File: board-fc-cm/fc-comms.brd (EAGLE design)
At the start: 95.9 x 90.2 mm, 258 parts, among them IC1 TXB0108PW, IC10 LNA_COMMON, IC12 TXB0108PW, IC2 LHA1+, IC3 MMZ09332BT1, IC4 PCT2075TP, IC5 PCT2075TP, IC6 MSP430FR2311PW, IC7 CC1125RHBT, IC8 CC1125RHBT, IC9 TXB0108PW, J1 SWD_SHROUD, Q1 8MHz, Q2 BSS84, Q3 32.768kHz, Q4 BSS123, Q5 BSS84, U1 TM4C123[7,G]XXPM, U2 TMP100-EP_DBV_6, U3 TPS3813K33-EP_DBV_6, U4 MPU-9250, U6 TPS79930QDDCRQ1, U7 TPS79930QDDCRQ1, U8 74LVC1G08, X1 BU-SMA-V, X10 BU-SMA-V, X11 BU-SMA-V, X12 BU-SMA-V, X14 BU-SMA-V, X15 BU-SMA-V, X16 BU-SMA-V, X17 BU-SMA-V, X18 SHIELD-26X26, X19 SHIELD-26X26, X2 BU-SMA-V, X20 LFTCXO070, X21 LFTCXO070, X3 BU-SMA-V, X4 BU-SMA-V, X5 BU-SMA-V, X6 BU-SMA-V, X7 BU-SMA-V, X8 BU-SMA-V, X9 BU-SMA-V

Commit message: more routing
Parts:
- moved R1 110.6 mm to (19.2, 80.4), turned to 270 degrees
- moved C95 10.5 mm to (60.8, 10.8)
- moved C50 5.26 mm to (62.0, 46.8), turned to 90 degrees
- moved C54 3.85 mm to (67.1, 29.9), turned to 0 degrees
- moved R22 3.79 mm to (52.0, 69.2), turned to 0 degrees
- moved R23 3.44 mm to (52.0, 70.8), turned to 0 degrees
- moved TP4 3.44 mm to (53.2, 63.2)
- moved C91 3.22 mm to (32.0, 70.8)
- moved C92 3.20 mm to (32.0, 72.8)
- moved C55 3.10 mm to (78.2, 47.2), turned to 180 degrees
- moved TP5 2.56 mm to (55.2, 63.2)
- moved C52 2.53 mm to (72.8, 47.2)
- moved C56 1.79 mm to (75.2, 47.2), turned to 0 degrees
- moved C7 1.44 mm to (62.0, 38.0), turned to 90 degrees
- moved C58 1.41 mm to (65.8, 49.0)
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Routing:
- net WDT_PA_EN: track 0.00 -> 142.8 mm, vias 0 -> 1
- net N$1: track 0.00 -> 142.1 mm, vias 0 -> 1
- net GND: track 139.8 -> 232.1 mm, vias 114 -> 160
- net TMP/SCL: track 0.00 -> 82.1 mm, vias 0 -> 6
- net TMP/SDA: track 0.00 -> 78.9 mm, vias 0 -> 5
- net RX_RST: track 11.5 -> 72.7 mm
- net RX_CLK: track 4.63 -> 64.7 mm
- net RX_MOSI: track 4.80 -> 63.9 mm, vias 2 -> 3
- net RX_MISO: track 6.86 -> 61.0 mm
- net TX_CS: track 12.6 -> 66.1 mm, vias 2 -> 3
- net RX_GPIO0: track 7.28 -> 58.2 mm, vias 2 -> 3
- net RX_CS: track 8.46 -> 59.3 mm
- net TX_RST: track 8.49 -> 56.1 mm, vias 2 -> 3
- net TC/TXRX/MISO: track 0.00 -> 44.3 mm, vias 0 -> 2
- net ANT/GATE: track 0.00 -> 42.4 mm, vias 0 -> 2
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- added copper zone on layer 1, net N$10
- added copper zone on layer 1, net N$3

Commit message: some more routing
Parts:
- removed C87, C88, C89, C90: dnp, passives-7351:C0603-N
- removed L18, L19, L20: 0R, passives-7351:L0603-N
- removed X16, X17: BU-SMA-V, con-coax:BU-SMA-V
- added R31, R32: 4k7, passives-7351:R0603-N
- moved C108 138.9 mm to (56.8, 59.6), turned to 180 degrees
- moved C10 130.8 mm to (56.0, 50.0), turned to 180 degrees
- moved TP16 104.3 mm to (34.3, 6.35), flipped to the bottom, turned to 270 degrees
- moved TP12 99.1 mm to (36.8, 6.35), flipped to the bottom, turned to 270 degrees
- moved TP14 98.1 mm to (31.8, 6.35), flipped to the bottom, turned to 270 degrees
- moved TP15 95.7 mm to (26.7, 6.35), flipped to the bottom, turned to 270 degrees
- moved TP13 93.9 mm to (29.2, 6.35), flipped to the bottom, turned to 270 degrees
- moved TP11 85.8 mm to (24.1, 6.35), flipped to the bottom, turned to 270 degrees
- moved R14 79.2 mm to (10.0, 80.8)
- moved R13 77.1 mm to (10.0, 79.2)
- moved R12 75.3 mm to (10.0, 77.6)
- moved R11 73.7 mm to (10.0, 76.0)
- moved SV5 72.5 mm to (55.6, 2.14), turned to 180 degrees
- moved LED2 64.8 mm to (18.2, 77.0), turned to 90 degrees
- moved LED4 59.9 mm to (6.80, 81.2), turned to 90 degrees
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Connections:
- removed net N$103: JP1.2, Q5.3
- removed net N$42: LED2.A, R12.1
- removed net N$58: R13.2
- removed net N$64: R12.2
- removed net N$65: R11.2
- removed net N$79: C87.2, L18.1, X16.1
- removed net N$80: C88.2, L18.2, L19.1
- removed net N$81: C89.2, L19.2, L20.1
- removed net N$82: C90.2, L20.2, X17.1
- removed net N$88: C98.1, C99.1, IC4.8, IC5.7, IC5.8, R22.2, R23.2
- new net N$2: C64.2, JP1.1, L11.2, LED7.A
- new net N$38: LED1.C, R11.2
- new net N$51: R13.2, U1.46
- net 3V3/FMCU: now also C98.1, C99.1, IC4.8, IC5.7, IC5.8, R22.2, R23.2
- net 3V3/SYS: now also R31.2, R32.2
- net 9AXIS/SCL: now also R32.1
- net 9AXIS/SDA: now also R31.1
- net GND: now also IC12.1, IC12.3, IC12.6, IC12.7, IC12.8, IC12.9, R11.1, R12.1; no longer C87.1, C88.1, C89.1, C90.1, LED1.C, LED2.C, X16.2, X16.3, X16.4, X16.5, X17.2, X17.3, X17.4, X17.5
- net N$41: now also LED2.C, R12.2; no longer LED1.A, R11.1
- net N$49: now also U1.50
- net N$52: now also JP1.2, Q5.3; no longer C64.2, JP1.1, L11.2, LED7.A
- net N$90: now also JP8.3; no longer JP8.4
- net N$91: now also JP8.4; no longer JP8.3
- net TX_GPIO3: now also LED2.A
- net WDT_PA_EN: now also LED1.A
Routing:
- net GND: track 232.1 -> 373.2 mm, vias 160 -> 232
- net 5V/SYS: track 9.59 -> 125.0 mm, vias 0 -> 8
- net 5V/CAM: track 0.00 -> 107.0 mm
- net 3V3/FMCU: track 30.9 -> 127.5 mm, vias 5 -> 12
- net PA_POWER: track 0.00 -> 95.3 mm, vias 0 -> 7
- net N$53: track 104.0 -> 199.2 mm, vias 13 -> 19
- net N$49: track 0.00 -> 93.9 mm, vias 0 -> 2
- net N$51: track 0.00 -> 90.2 mm, vias 0 -> 2
- net N$40: track 112.6 -> 201.7 mm, vias 17 -> 24
- net N$61: track 0.00 -> 80.5 mm, vias 0 -> 2
- net TX_GPIO3: track 2.00 -> 82.4 mm, vias 1 -> 2
- net N$73: track 0.00 -> 79.5 mm, vias 0 -> 2
- net RX_GPIO3: track 2.09 -> 81.3 mm, vias 1 -> 2
- net TX_REG_EN: track 7.76 -> 82.1 mm, vias 1 -> 4
- net SWDIO: track 34.5 -> 88.6 mm, vias 1 -> 3
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- added copper zone on layer 15, net 3V3/FMCU
- added copper zone on layer 15, net 5V/SYS
- added copper zone on layer 2, net 5V/SYS
- added copper zone on layer 2, net GND
- added copper zone on layer 15, net N$24
- added copper zone on layer 15, net N$40
- added copper zone on layer 15, net PA_PWR
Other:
- board text added: "5V"
- board text added: "CAM"
- board text added: "GPIO3"
- board text added: "LNA FET BYPASS"
- board text added: "LNA PWR"
- board text added: "PA"
- board text added: "PA FET BYPASS"
- board text added: "PA PWR"
- board text added: "SYS"
- board text added: "WDT PA EN"

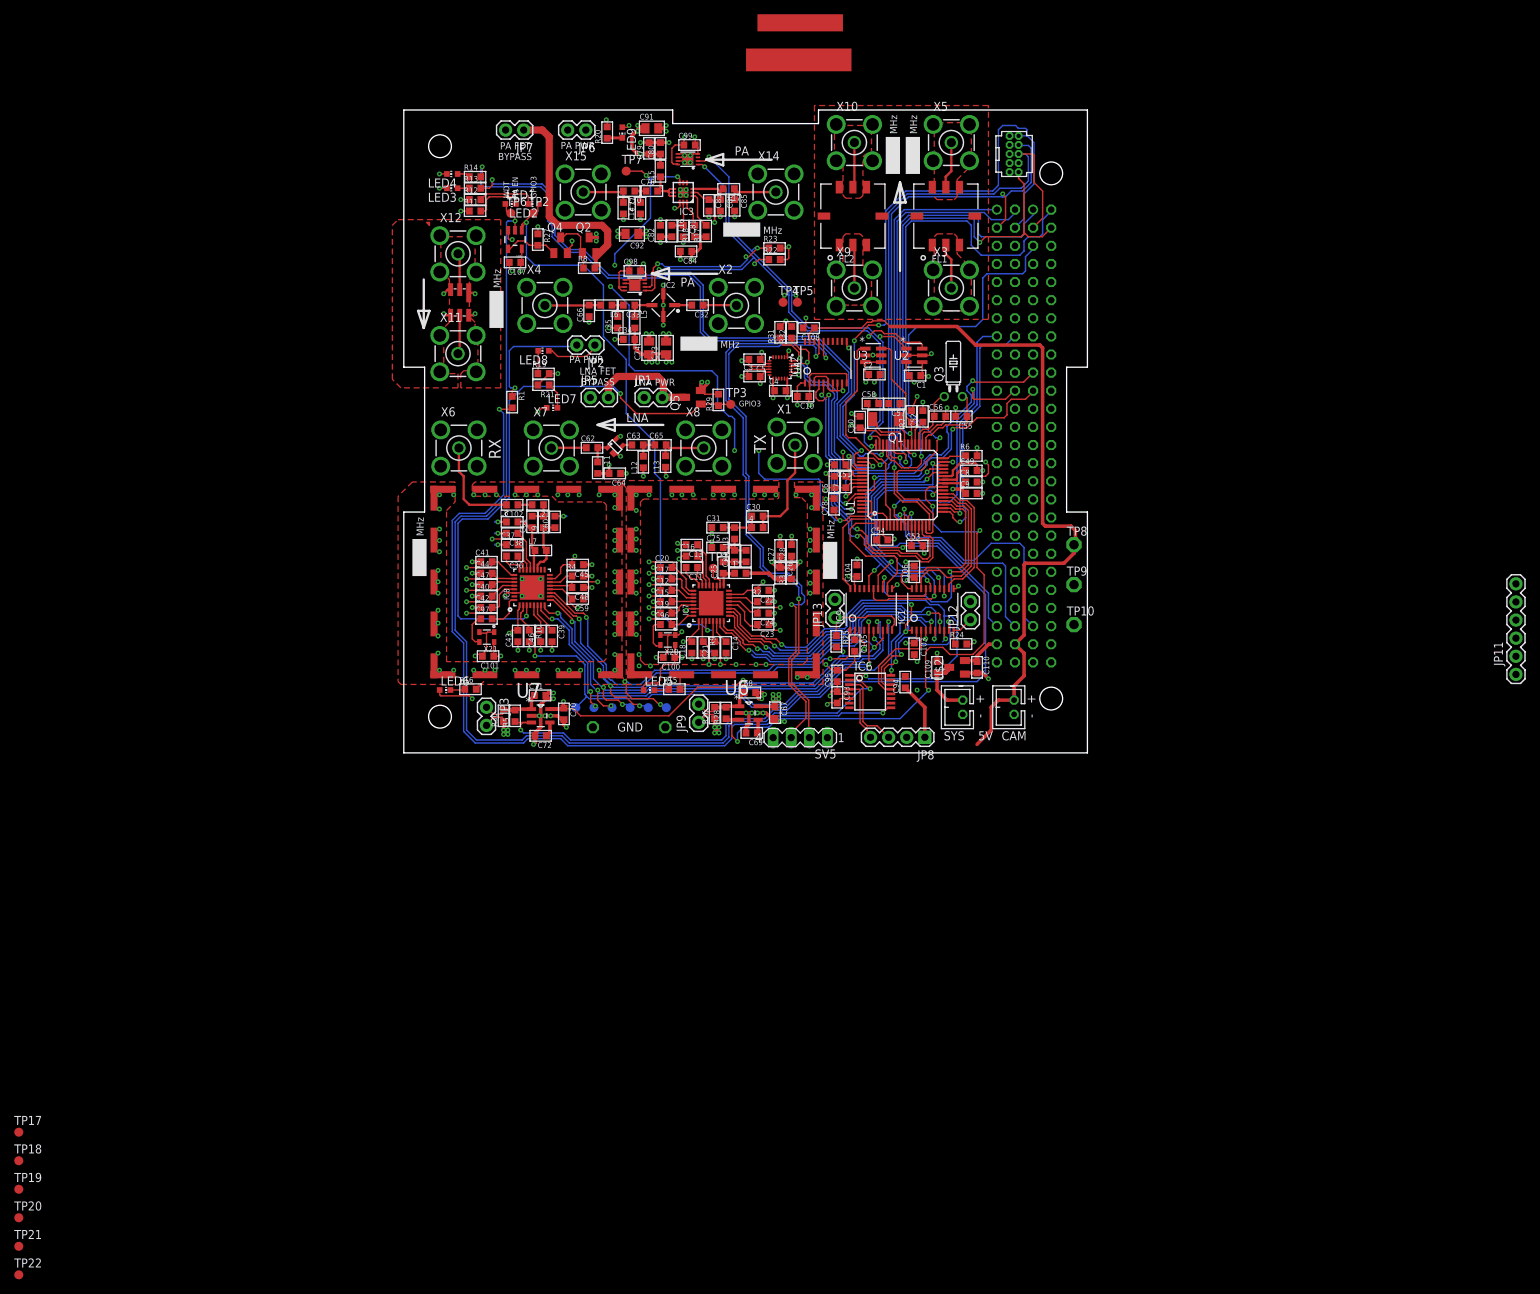
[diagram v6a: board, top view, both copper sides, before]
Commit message: cleaning up silk
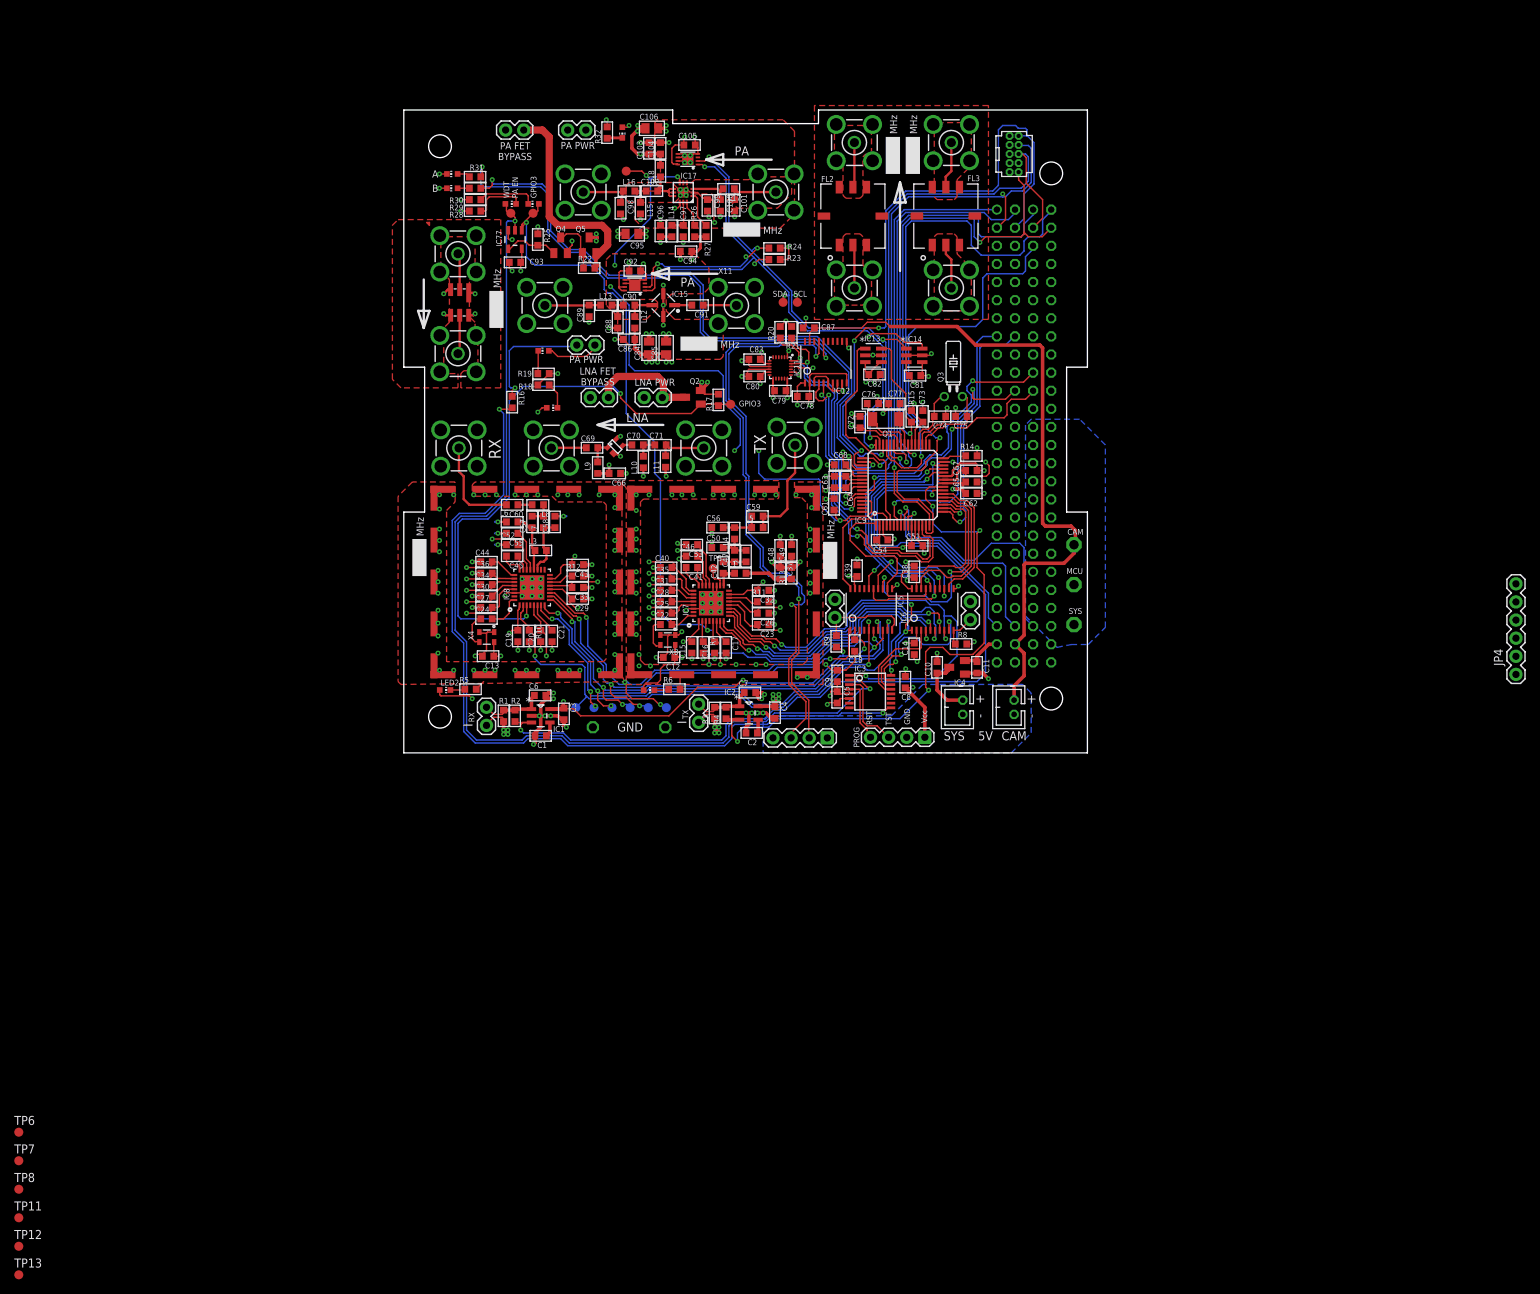
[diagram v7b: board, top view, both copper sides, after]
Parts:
- removed C107: 100n, passives-7351:C0603-N
- removed C109, C110: 4.7u, passives-7351:C0603-N
- removed JP13: M02PTH, SparkFun-Connectors:1X02
- removed L21: 15n, passives-7351:L0603-N
- removed SV5: CAM, con-lstb:MA04-1
- removed U$2: MCP1700TT, dtb:SOT23
- removed U1: TM4C123[7,G]XXPM, ti-tiva:PM_S-PQFP-G64
- removed U6, U7: TPS79930QDDCRQ1, cube-parts:SOT95P280X110-5N
- removed X19: SHIELD-26X26, CubeSat3:SHIELD-26X26
- removed X20, X21: LFTCXO070, CubeSat3:260-SERIES
- added C88, C89: dnp, passives-7351:C0603-N
- added C90: ??, passives-7351:C0603-N
- added IC15: LHA1+, CubeSat3:PA
- added IC16, IC18: PCT2075TP, CubeSat3:HWSON8
- added IC17: MMZ09332BT1, CubeSat3:QFN3X3-6
- added JP10: M02PTH, SparkFun-Connectors:1X02
- added JP4: FTDI_BASICPTH, SparkFun-Connectors:FTDI_BASIC
- added L18: 33n, passives-7351:L0603-N
- added X13, X16, X17: BU-SMA-V, con-coax:BU-SMA-V
- C1, C2: value 0.1u -> 10n
- C10: value 0.1u -> 4.7u
- C100: value 100n -> 27p
- C101: value 100n -> 15p
- C102: value (none) -> 220p
- C103: value 100n -> 4.7u
- C104: value 100n -> 1n
- C106, C95: value 100n -> (none); device passives-7351:C0603-N -> passives-7351:C0805-N
- C11: value 1.8n -> 4.7u
- C12, C18: value 47n -> 100n
- C13, C38: value 10n -> 100n
- C14, C39: value 220n -> 100n
- C17, C21: value 47n -> 220n
- C22, C24: value 47n -> 10n
- C25: value 82p -> 47n
- C26, C27: value 100p -> 47n
- C28: value 10n -> 47n
- C29: value 12p -> 47n
- C3, C4, C6, C7: value 0.1u -> 2u2
- C30: value 1.2p -> 47n
- C31: value 15p -> 47n
- C32: value 1n -> 47n
- C33, C34: value ?? -> 47n
- C35: value dnp -> 47n
- C36: value 1.8n -> 47n
- C37, C48: value 47n -> 100p
- C41, C45: value 47n -> 1.8n
- C42: value 47n -> 82p
- C47: value 47n -> 12p
- C49, C53: value 0.01u -> 10n
- C5: value 0.01u -> 1u
- C50: value 0.1u -> 12p
- C52: value 0.1u -> 47n
- C55: value 24p -> 10n
- C56: value 24p -> 15p
- C57, C58: value 10p -> 5.1p
- C59: value 47n -> 1.2p
- C60: value 5.1p -> (none)
- C61: value 5.1p -> 100p
- C62: value ?? -> 2.2u
- C63, C64: value ?? -> 0.1u
- C65: value 0R -> 1.0u
- C66: value dnp -> ??
- C67, C68: value 2u2 -> 0.01u
- C69: value 10n -> ??
- C70: value 2u2 -> ??
- C71: value 2u2 -> 0R
- C72: value 10n -> 0.1u
- C73: value (none) -> 0.1u; device passives-7351:C0805-N -> passives-7351:C0603-N
- C74: value (none) -> 24p; device passives-7351:C0805-N -> passives-7351:C0603-N
- C75: value 12p -> 24p
- C76: value 220p -> 10p
- C77: value 33p -> 10p
- C78: value 100p -> 0.1u
- C79: value 4.7u -> 0.1u
- C8: value 1.0u -> 1u
- C80: value 1n -> 0.1u
- C81: value 3.3p -> 0.1u
- C82: value 1u -> 0.1u
- C83: value 100p -> 0.01u
- C84: value 1u -> (none); device passives-7351:C0603-N -> passives-7351:C0805-N
- C85: value 15p -> (none); device passives-7351:C0603-N -> passives-7351:C0805-N
- C86: value 27p -> ??
- C9: value 2.2u -> 100n
- C91: value (none) -> 1n; device passives-7351:C0805-N -> passives-7351:C0603-N
- C92: value (none) -> 100n; device passives-7351:C0805-N -> passives-7351:C0603-N
- C93: value 1u -> 100n
- C96: value 10n -> 1u
- C97: value 10n -> 3.3p
- C98: value 100n -> 33p
- C99: value 100n -> 100p
- FL1: value LPF_CS -> GOLLEDGE_SAW_FILTER; device CubeSat3:PL-176 -> Ava:GOLLEDGE_SAW
- FL3: value GOLLEDGE_SAW_FILTER -> LPF_CS; device Ava:GOLLEDGE_SAW -> CubeSat3:PL-176
- IC1: value TXB0108PW -> TPS79930QDDCRQ1; device cube-parts:TSSOP20 -> cube-parts:SOT95P280X110-5N
- IC2: value LHA1+ -> TPS79930QDDCRQ1; device CubeSat3:PA -> cube-parts:SOT95P280X110-5N
- IC3: value MMZ09332BT1 -> MSP430FR2311PW; device CubeSat3:QFN3X3-6 -> CubeSat3:SSOP16
- IC4: value PCT2075TP -> MCP1700TT; device CubeSat3:HWSON8 -> dtb:SOT23
- IC5: value PCT2075TP -> TXB0108PW; device CubeSat3:HWSON8 -> cube-parts:TSSOP20
- IC6: value MSP430FR2311PW -> TXB0108PW; device CubeSat3:SSOP16 -> cube-parts:TSSOP20
- IC9: value TXB0108PW -> TM4C123[7,G]XXPM; device cube-parts:TSSOP20 -> ti-tiva:PM_S-PQFP-G64
- J1: value SWD_SHROUD -> (none); device dtb:SWD_PTH_SHROUD -> dtb:JST-2-TH
- J3: value (none) -> SWD_SHROUD; device dtb:JST-2-TH -> dtb:SWD_PTH_SHROUD
- JP1, JP12: value M02PTH -> (none); device SparkFun-Connectors:1X02 -> SparkFun-Connectors:1X04
- JP11: value FTDI_BASICPTH -> M02PTH; device SparkFun-Connectors:FTDI_BASIC -> SparkFun-Connectors:1X02
- JP8: value (none) -> M02PTH; device SparkFun-Connectors:1X04 -> SparkFun-Connectors:1X02
- L10: value 33n -> dnp
- L11: value ?? -> dnp
- L12: value dnp -> 220n
- L13: value dnp -> 0R
- L3: value 100n -> 56n
- L4: value 68n -> 100n
- L5: value 220n -> 68n
- L6: value 0R -> 27n
- L7: value 56n -> 27u
- L8: value 27n -> 15n
- L9: value 27u -> ??
- R1: value 10k -> 0.2
- R11, R12: value (none) -> 56k 0.5%
- R13: value (none) -> 22
- R14: value (none) -> 1M
- R15, R16: value (none) -> 10k
- R17: value 2.2k -> 100k
- R18: value 1.8k -> (none)
- R2, R4: value 56k 0.5% -> 10k
- R20, R21: value (none) -> 4k7
- R22: value 4k7 -> 100k
- R24: value 10k -> 4k7
- R26: value 0.2 -> 1.8k
- R27: value 10k -> 2.2k
- R28, R5: value 10k -> (none)
- R29: value 100k -> (none)
- R3: value 22 -> 0.2
- R30: value 0.2 -> (none)
- R31, R32: value 4k7 -> (none)
- R6: value 1M -> (none)
- R7: value 10k -> 100k
- R8, R9: value 100k -> 10k
- TP1, TP2, TP4: value PTR1B1,27 -> PTR1PAD1-13; device testpad:B1,27 -> testpad:P1-13
- TP10, TP8, TP9: value PTR1PAD1-13 -> PTR1B1,27; device testpad:P1-13 -> testpad:B1,27
- X1, X2: value BU-SMA-V -> SHIELD-26X26; device con-coax:BU-SMA-V -> CubeSat3:SHIELD-26X26
- X18: value SHIELD-26X26 -> BU-SMA-V; device CubeSat3:SHIELD-26X26 -> con-coax:BU-SMA-V
- X3, X4: value BU-SMA-V -> LFTCXO070; device con-coax:BU-SMA-V -> CubeSat3:260-SERIES
- moved TP8 173.4 mm to (-54.0, -61.2)
- moved TP7 162.9 mm to (-54.0, -57.2)
- moved JP11 151.2 mm to (25.5, 87.4), turned to 180 degrees
- moved TP6 146.2 mm to (-54.0, -53.2)
- moved TP22 120.7 mm to (36.8, 6.35), flipped to the bottom, turned to 270 degrees
- moved TP12 118.1 mm to (-54.0, -69.2), flipped to the top, turned to 0 degrees
- moved TP21 116.2 mm to (34.3, 6.35), flipped to the bottom, turned to 270 degrees
- moved TP13 115.1 mm to (-54.0, -73.2), flipped to the top, turned to 0 degrees
- moved TP20 111.7 mm to (31.8, 6.35), flipped to the bottom, turned to 270 degrees
- moved TP19 107.2 mm to (29.2, 6.35), flipped to the bottom, turned to 270 degrees
- moved TP11 105.9 mm to (-54.0, -65.2), flipped to the top, turned to 0 degrees
- moved TP18 102.7 mm to (26.7, 6.35), flipped to the bottom, turned to 270 degrees
- moved TP17 98.2 mm to (24.1, 6.35), flipped to the bottom, turned to 270 degrees
- moved TP2 92.0 mm to (94.0, 23.6)
- moved X18 87.8 mm to (76.8, 85.6)
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- renumbered C108 to C87, SV16 to SV2, SV17 to SV3, U2 to IC14, U3 to IC13, U4 to IC11, U8 to IC77
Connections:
- net !RST: now also IC9.38, J3.10, R15.1; no longer J1.10, R7.1, U1.38
- net !WAKE: now also IC9.32, R14.1; no longer R6.1, U1.32
- net +5V: now also JP10.1, Q5.2, R22.2; no longer JP7.1, Q2.2, R8.2
- net 3V3/FMCU: now also C105.1, C11.1, C38.1, C39.1, C67.1, C68.1, C72.1, C73.1, C78.1, C79.1, C81.1, C82.1, C83.1, C92.1, IC11.1, IC11.13, IC11.22, IC11.8, IC13.3, IC13.4, IC14.4, IC16.7, IC16.8, IC18.8, IC4.2, IC5.19, IC6.19, IC9.11, IC9.2, IC9.26, IC9.37, IC9.42, IC9.54, J3.1, R14.2, R15.2, R20.2, R21.2, R24.2, TP2.TP; no longer C10.1, C104.1, C106.1, C110.1, C49.1, C50.1, C52.1, C53.1, C98.1, C99.1, IC1.19, IC4.8, IC5.7, IC5.8, IC9.19, J1.1, R22.2, R6.2, R7.2, TP9.TP, U$2.2, U1.11, U1.2, U1.26, U1.37, U1.42, U1.54
- net 3V3/SYS: no longer C1.1, C2.1, C4.1, C5.1, IC11.1, IC11.13, IC11.22, IC11.8, IC13.3, IC13.4, IC14.4, R31.2, R32.2
- net 5V/CAM: now also J2.1, JP12.4, TP4.TP; no longer J3.1, SV5.4, TP8.TP
- net 5V/SYS: now also C10.1, IC4.3, J1.1, JP2.1, R1.1, R3.1, TP1.TP; no longer C109.1, J2.1, JP9.1, R26.1, R30.1, TP10.TP, U$2.3
- net 9AXIS/SCL: now also IC9.59, R21.1; no longer R32.1, U1.59
- net 9AXIS/SDA: now also IC9.60, R20.1; no longer R31.1, U1.60
- net ANT/GATE: now also IC9.57; no longer U1.57
- net ANT/SW: now also IC9.58; no longer U1.58
- net CAM/RXD: now also IC9.13; no longer U1.13
- net CAM/TXD: now also IC9.14; no longer U1.14
- net EWFEWF: now also C6.1, IC1.1, R1.2, R2.2; no longer C71.1, R30.2, R5.2, U7.1
- net GND: now also C11.2, C12.2, C17.2, C18.2, C21.2, C25.1, C26.1, C27.1, C28.1, C29.1, C30.1, C32.1, C33.1, C36.1, C48.2, C50.1, C52.1, C56.1, C61.2, C62.2, C63.2, C64.2, C65.2, C75.2, C76.2, C86.1, C88.1, C89.1, C96.2, C97.2, FL1.A, FL1.C, FL1.D, FL1.F, FL3.1, FL3.3, FL3.4, FL3.5, FL3.7, FL3.8, IC1.2, IC15.GND1, IC15.GND2, IC16.4, IC16.5, IC16.6, IC16.EP, IC17.10, IC17.EXP, IC18.4, IC18.5, IC18.6, IC18.7, IC18.EP, IC2.2, IC3.6, IC4.1, IC5.11, IC6.11, IC9.12, IC9.27, IC9.3, IC9.35, IC9.39, IC9.55, J1.2, J3.3, J3.5, J3.9, JP1.2, JP12.1, JP4.GND, JP5.2, JP6.2, L10.1, L11.1, L15.1, L6.1, LED7.C, LED8.C, R11.2, R12.2, R18.2, R25.1, R28.1, R29.1, R32.2, R5.2, R6.2, X1.G1, X1.G10, X1.G11, X1.G12, X1.G13, X1.G14, X1.G15, X1.G16, X1.G17, X1.G19, X1.G2, X1.G20, X1.G21, X1.G3, X1.G4, X1.G5, X1.G6, X1.G7, X1.G8, X1.G9, X13.2, X13.3, X13.4, X13.5, X16.2, X16.3, X16.4, X16.5, X17.2, X17.3, X17.4, X17.5, X18.2, X18.3, X18.4, X18.5, X2.G1, X2.G10, X2.G11, X2.G12, X2.G13, X2.G14, X2.G15, X2.G16, X2.G17, X2.G19, X2.G2, X2.G20, X2.G21, X2.G3, X2.G4, X2.G5, X2.G6, X2.G7, X2.G8, X2.G9, X3.1, X4.1; no longer C107.2, C109.2, C110.2, C12.1, C17.1, C18.1, C21.1, C22.1, C24.1, C27.2, C28.2, C37.1, C41.1, C42.1, C45.1, C47.1, C48.1, C50.2, C52.2, C56.2, C57.2, C59.1, C60.2, C64.1, C69.2, C70.2, C71.2, C75.1, C86.2, C91.2, FL1.1, FL1.3, FL1.4, FL1.5, FL1.7, FL1.8, FL3.A, FL3.C, FL3.D, FL3.F, IC1.11, IC2.GND1, IC2.GND2, IC3.10, IC3.EXP, IC4.4, IC4.5, IC4.6, IC4.7, IC4.EP, IC5.4, IC5.5, IC5.6, IC5.EP, IC6.6, IC9.11, J1.3, J1.5, J1.9, J3.2, JP11.GND, JP12.2, JP13.2, JP8.2, L12.1, L13.1, L14.1, L8.1, LED3.C, LED4.C, R11.1, R12.1, R15.2, R16.2, R2.2, R20.2, R21.2, R27.1, R4.2, SV5.1, U$2.1, U1.12, U1.27, U1.3, U1.35, U1.39, U1.55, U6.2, U7.2, X1.2, X1.3, X1.4, X1.5, X18.G1, X18.G10, X18.G11, X18.G12, X18.G13, X18.G14, X18.G15, X18.G16, X18.G17, X18.G19, X18.G2, X18.G20, X18.G21, X18.G3, X18.G4, X18.G5, X18.G6, X18.G7, X18.G8, X18.G9, X19.G1, X19.G10, X19.G11, X19.G12, X19.G13, X19.G14, X19.G15, X19.G16, X19.G17, X19.G19, X19.G2, X19.G20, X19.G21, X19.G3, X19.G4, X19.G5, X19.G6, X19.G7, X19.G8, X19.G9, X2.2, X2.3, X2.4, X2.5, X20.1, X20.3, X21.1, X21.3, X3.2, X3.4, X3.5, X4.2, X4.4, X4.5
- net GNSS/!RESETIN: now also IC9.6; no longer U1.6
- net GNSS/PV: now also IC9.7; no longer U1.7
- net GNSS/RXD: now also IC9.18; no longer U1.18
- net GNSS/TXD: now also IC9.17; no longer U1.17
- net GPIO1: now also IC9.16; no longer U1.16
- net GPIO2: now also IC9.43; no longer U1.43
- net GPIO3: now also IC9.44; no longer U1.44
- net GPIO4: now also IC9.45; no longer U1.45
- net GPIO5: now also IC9.15; no longer U1.15
- net N$1: now also IC3.9, R16.2; no longer IC6.9, R1.2
- net N$101: now also C60.2, X5.1; no longer C102.2, X6.1
- net N$102: now also C7.1, IC2.1, JP2.2, R3.2, R4.2; no longer C68.1, JP9.2, R26.2, R28.2, U6.1
- net N$11: now also C53.1; no longer C13.1
- net N$117: now also R25.2; no longer R27.2
- net N$12: now also C42.1; no longer C25.1
- net N$13: now also R11.1; no longer R2.1
- net N$14: now also C22.2; no longer C96.2
- net N$15: now also C37.2, R13.1; no longer C26.2, R3.1
- net N$16: now also C91.2, IC15.RF_IN; no longer C32.2, IC2.RF_IN
- net N$17: now also C69.1, X6.1; no longer C62.1, X7.1
- net N$18: now also C90.1, IC15.RF_OUT, L12.1; no longer C33.1, IC2.RF_OUT, L5.1
- net N$19: now also C17.1; no longer C14.1
- net N$2: now also C66.2, JP8.1, L9.2, LED3.A; no longer C64.2, JP1.1, L11.2, LED7.A
- net N$20: now also C42.2, C47.1; no longer C25.2, C29.1
- net N$21: now also C47.2, C50.2, L4.1; no longer C29.2, C75.2, L3.1
- net N$22: now also C56.2, C59.1, L4.2, L5.1; no longer C30.1, C31.2, L3.2, L4.1
- net N$23: now also C59.2, L5.2, X8.1; no longer C30.2, L4.2, X1.1
- net N$24: now also C103.1, C104.1, C106.1, C94.1, C95.1, C96.1, C99.1, IC17.2, JP11.1, L14.2, L18.2, R26.1, R27.1; no longer C79.1, C80.1, C82.1, C83.1, C84.1, C91.1, C92.1, IC3.2, JP6.1, L15.2, L16.2, R17.1, R18.1
- net N$25: now also C69.2, L9.1; no longer C62.2, L11.1
- net N$26: now also C91.1, X11.1; no longer C32.1, X2.1
- net N$27: now also C88.2, C90.2, L13.1; no longer C33.2, C35.2, L6.1
- net N$28: now also FL3.2, X13.1; no longer FL1.2, X3.1
- net N$29: now also FL3.6, X18.1; no longer FL1.6, X5.1
- net N$30: now also C45.1; no longer C36.1
- net N$31: now also C45.2; no longer C36.2
- net N$32: now also C55.1; no longer C38.1
- net N$33: now also C76.1, IC9.41; no longer C58.1, U1.41
- net N$34: now also C74.1, IC9.36; no longer C56.1, U1.36
- net N$35: now also R12.1; no longer R4.1
- net N$36: now also C24.2; no longer C97.2
- net N$37: now also C89.2, L13.2, X10.1; no longer C66.2, L6.2, X4.1
- net N$38: now also LED5.C, R28.2; no longer LED1.C, R11.2
- net N$39: now also TP3.TP; no longer TP1.TP
- net N$4: now also C80.1; no longer C3.1
- net N$40: now also C12.1, C14.1, C25.2, C26.2, C28.2, C31.2, C32.2, C35.2, C37.1, C4.1, C40.2, C46.2, C48.1, C49.1, C5.1, C8.1, C9.1, IC2.5, IC3.5, IC6.2, JP1.1, LED1.A, R13.2, R7.2, R8.2, X3.6; no longer C100.1, C103.1, C107.1, C12.2, C17.2, C18.2, C19.2, C20.2, C21.2, C22.2, C24.2, C26.1, C27.1, C28.1, C67.1, C94.1, C95.1, IC1.2, IC6.5, JP8.1, LED5.A, R24.2, R3.2, R9.2, U6.5, X20.6
- net N$41: now also LED6.C, R29.2; no longer LED2.C, R12.2
- net N$43: now also LED7.A, R30.1; no longer LED3.A, R13.1
- net N$44: now also LED8.A, R31.1; no longer LED4.A, R14.1
- net N$45: now also C21.1; no longer C39.1
- net N$46: now also C70.1; no longer C63.1
- net N$47: now also C58.1, L3.2, L7.1; no longer C60.1, L7.2, L9.1
- net N$48: now also C57.1, L3.1, L6.2; no longer C61.1, L7.1, L8.2
- net N$49: now also IC9.50, R31.2; no longer R14.2, U1.50
- net N$5: now also C62.1, C63.1, C64.1, C65.1, IC9.25, IC9.56; no longer C6.1, C7.1, C8.1, C9.1, U1.25, U1.56
- net N$50: now also C70.2, C71.1, L10.2; no longer C63.2, C65.1, L12.2
- net N$51: now also IC9.46, R30.2; no longer R13.2, U1.46
- net N$52: now also JP7.2, JP8.2, Q2.3; no longer JP1.2, JP5.2, Q5.3
- net N$53: now also C13.1, C18.1, C19.2, C20.2, C27.2, C29.2, C3.1, C30.2, C33.2, C34.2, C36.2, C52.2, IC1.5, IC5.2, JP7.1, LED2.A, Q2.2, R17.2, R9.2, X4.6; no longer C101.1, C105.1, C37.2, C40.2, C41.2, C42.2, C45.2, C46.2, C47.2, C48.2, C59.2, C70.1, IC9.2, JP5.1, LED6.A, Q5.2, R25.2, R29.2, U7.5, X21.6
- net N$54: now also C71.2, L11.2, X7.1; no longer C65.2, L13.2, X8.1
- net N$55: now also X12.1; no longer X9.1
- net N$56: now also X17.1; no longer X10.1
- net N$57: now also C2.1, IC2.4; no longer C69.1, U6.4
- net N$6: now also C75.1, IC9.34; no longer C55.1, U1.34
- net N$60: now also C1.1, IC1.4; no longer C72.1, U7.4
- net N$61: now also JP12.3; no longer SV5.3
- net N$62: now also Q5.1, R22.1; no longer Q2.1, R8.1
- net N$66: now also LED1.C, R6.1; no longer LED5.C, R15.1
- net N$67: now also LED2.C, R5.1; no longer LED6.C, R16.1
- net N$68: now also FL1.E, X9.1; no longer FL3.E, X11.1
- net N$69: now also FL1.B, X14.1; no longer FL3.B, X12.1
- net N$7: now also C41.1; no longer C11.1
- net N$70: now also C102.1, L15.2, L16.1; no longer C76.1, L10.1, L14.2
- net N$71: now also C102.2, IC17.7, IC17.8, IC17.9, L18.1; no longer C76.2, IC3.7, IC3.8, IC3.9, L15.1
- net N$72: now also C98.1, L16.2; no longer C77.1, L10.2
- net N$73: now also JP12.2; no longer SV5.2
- net N$74: now also C97.1, IC17.11, L14.1; no longer C81.1, IC3.11, L16.1
- net N$75: now also IC17.12, R26.2; no longer IC3.12, R18.2
- net N$76: now also IC17.1, R27.2; no longer IC3.1, R17.2
- net N$77: now also C101.1, X16.1; no longer C85.1, X14.1
- net N$78: now also C100.1, IC17.3; no longer C86.1, IC3.3
- net N$8: now also C77.1, IC9.40; no longer C57.1, U1.40
- net N$83: now also C84.1, C85.1, C86.2, JP9.1, L12.2, LED4.A; no longer C34.2, C73.1, C74.1, JP2.1, L5.2, LED8.A
- net N$84: now also LED4.C; no longer LED8.C
- net N$85: now also R32.1; no longer R20.1
- net N$86: now also LED3.C, R18.1; no longer LED7.C, R21.1
- net N$87: now also C22.1, X3.4; no longer C96.1, X20.4
- net N$89: now also C24.1, X4.4; no longer C97.1, X21.4
- net N$9: now also C41.2; no longer C11.2
- net N$90: now also IC3.3, JP1.3; no longer IC6.3, JP8.3
- net N$91: now also IC3.4, JP1.4; no longer IC6.4, JP8.4
- net N$92: now also IC3.11, JP4.TXO; no longer IC6.11, JP11.TXO
- net N$93: now also IC3.10, JP4.RXI; no longer IC6.10, JP11.RXI
- net N$94: now also C60.1, L8.2; no longer C102.1, L21.2
- net N$95: now also C57.2, L7.2, L8.1; no longer C61.2, L21.1, L9.2
- net N$98: now also IC6.10, JP5.1, R8.1; no longer IC1.10, JP12.1, R24.1
- net N$99: now also IC5.10, JP6.1, R9.1; no longer IC9.10, JP13.1, R25.1
- net PA_POWER: now also C61.1, IC17.6, IC9.61, TP16.TP; no longer C78.1, IC3.6, TP7.TP, U1.61
- net PA_PWR: now also JP10.2, JP11.2, JP9.2, Q5.3, R16.1; no longer JP2.2, JP6.2, JP7.2, Q2.3, R1.1
- net PWR/INT: now also IC9.10; no longer U1.10
- net PWR/RXD: now also IC9.8; no longer U1.8
- net PWR/TXD: now also IC9.9; no longer U1.9
- net RX/GPIO0: now also IC5.20, IC9.4; no longer IC9.20, U1.4
- net RX_CLK: now also IC5.7, TP19.TP; no longer IC9.7, TP13.TP
- net RX_CS: now also IC5.8, TP22.TP; no longer IC9.8, TP12.TP
- net RX_GPIO0: now also IC5.1, TP21.TP; no longer IC9.1, TP16.TP
- net RX_GPIO3: now also Q2.1, R17.1, TP5.TP; no longer Q5.1, R29.1, TP3.TP
- net RX_MISO: now also IC5.6, TP20.TP; no longer IC9.6, TP14.TP
- net RX_MOSI: now also IC5.5, TP18.TP; no longer IC9.5, TP15.TP
- net RX_REG_EN: now also IC1.3, IC9.23, R2.1; no longer R5.1, U1.23, U7.3
- net RX_RST: now also IC5.9, TP17.TP; no longer IC9.9, TP11.TP
- net SWCLK: now also IC9.52, J3.4; no longer J1.4, U1.52
- net SWDIO: now also IC9.51, J3.2; no longer J1.2, U1.51
- net SWO: now also IC9.49, J3.6; no longer J1.6, U1.49
- net TC/RX/CS: now also IC5.13, IC9.20; no longer IC9.13, U1.20
- net TC/TX/CS: now also IC6.13, IC9.31; no longer IC1.13, U1.31
- net TC/TXRX/CLK: now also IC5.14, IC6.14, IC9.30; no longer IC1.14, IC9.14, U1.30
- net TC/TXRX/MISO: now also IC5.15, IC6.15, IC9.28; no longer IC1.15, IC9.15, U1.28
- net TC/TXRX/MOSI: now also IC5.16, IC6.16, IC9.29; no longer IC1.16, IC9.16, U1.29
- net TC/TXRX/RST: now also IC5.12, IC6.17, IC9.1; no longer IC1.17, IC9.12, U1.1
- net TMP/SCL: now also IC16.2, IC18.2, IC9.47, R24.1, TP10.TP; no longer IC4.2, IC5.2, R23.1, TP5.TP, U1.47
- net TMP/SDA: now also IC16.1, IC18.1, IC9.48, R23.1, TP9.TP; no longer IC4.1, IC5.1, R22.1, TP4.TP, U1.48
- net TX/GPIO0: now also IC6.20, IC9.19; no longer IC1.20, U1.19
- net TX/WDT/ACK: now also IC6.18, IC9.21; no longer IC1.18, U1.21
- net TX/WDT/ERR: now also IC6.12, IC9.22; no longer IC1.12, U1.22
- net TX_CLK: now also IC6.7, TP8.TP; no longer IC1.7, TP19.TP
- net TX_CS: now also IC3.1, IC6.8, TP7.TP; no longer IC1.8, IC6.1, TP18.TP
- net TX_GPIO0: now also IC3.15, IC6.1, TP13.TP; no longer IC1.1, IC6.15, TP22.TP
- net TX_GPIO3: now also LED6.A, TP15.TP; no longer LED2.A, TP2.TP
- net TX_MISO: now also IC6.6, TP12.TP; no longer IC1.6, TP21.TP
- net TX_MOSI: now also IC6.5, TP11.TP; no longer IC1.5, TP20.TP
- net TX_REG_EN: now also IC2.3, IC9.24, R4.1; no longer R28.1, U1.24, U6.3
- net TX_RST: now also IC3.16, IC6.4, R7.1, TP6.TP; no longer IC1.4, IC6.16, R9.1, TP17.TP
- net WDT/KICK: now also IC9.5; no longer U1.5
- net WDT_ACK: now also IC3.13, IC6.3; no longer IC1.3, IC6.13
- net WDT_ERR: now also IC3.14, IC6.9; no longer IC1.9, IC6.14
- net WDT_PA_EN: now also IC3.2, LED5.A, TP14.TP; no longer IC6.2, LED1.A, TP6.TP
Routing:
- net 3V3/FMCU: track 127.5 -> 154.1 mm, vias 12 -> 19
- net 3V3/SYS: track 25.1 -> 2.54 mm, vias 7 -> 0
- net 5V/SYS: track 125.0 -> 106.0 mm
- net GND: track 373.2 -> 357.6 mm, vias 232 -> 247
- net 5V/CAM: track 107.0 -> 97.2 mm
- net N$24: track 34.9 -> 42.2 mm
- net TX_RST: track 50.6 -> 55.3 mm
- net N$53: track 199.2 -> 203.8 mm, vias 19 -> 20
- net N$40: track 201.7 -> 202.9 mm
- net RX_GPIO0: track 64.8 -> 63.6 mm
- net TX_GPIO3: track 82.4 -> 83.4 mm
- net PA_POWER: track 95.3 -> 96.2 mm
- net N$49: track 93.9 -> 93.1 mm
- net TX_MOSI: track 38.5 -> 37.7 mm
- net SWO: track 78.6 -> 78.0 mm
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- added copper zone on layer 16, net 5V/CAM
- added copper zone on layer 16, net 5V/SYS
- added copper zone on layer 1, net N$42
- added copper zone on layer 1, net N$58
- added copper zone on layer 1, net N$59
- removed copper zone on layer 2, net 5V/SYS
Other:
- board text added: "!CS"
- board text added: "A"
- board text added: "B"
- board text added: "CLK"
- board text added: "GND"
- board text added: "GPIO0"
- board text added: "I"
- board text added: "MCU"
- board text added: "MISO"
- board text added: "MOSI"
- board text added: "PROG"
- board text added: "RST"
- board text added: "SCL"
- board text added: "SDA"
- board text added: "TST"
- board text added: "Vcc"

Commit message: almost done
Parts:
- removed C8: 1u, passives-7351:C0603-N
- removed JP4: FTDI_BASICPTH, SparkFun-Connectors:FTDI_BASIC
- added TP23, TP24, TP25: PTR1B1,27, testpad:B1,27
- moved TP13 140.7 mm to (54.3, 16.6), flipped to the bottom
- moved TP12 136.2 mm to (51.8, 16.6), flipped to the bottom
- moved TP7 133.1 mm to (56.8, 16.6), flipped to the bottom
- moved TP11 129.7 mm to (46.7, 16.6), flipped to the bottom
- moved TP8 129.2 mm to (49.2, 16.6), flipped to the bottom
- moved TP6 120.4 mm to (44.1, 16.6), flipped to the bottom
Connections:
- net GND: now also TP25.TP; no longer C8.2, JP4.GND
- net N$40: no longer C8.1
- net N$92: now also TP24.TP; no longer JP4.TXO
- net N$93: now also TP23.TP; no longer JP4.RXI
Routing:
- net N$92: track 0.00 -> 19.2 mm, vias 0 -> 1
- net N$93: track 0.00 -> 14.8 mm, vias 0 -> 1
- net 5V/SYS: track 106.0 -> 96.0 mm
- net GND: track 357.6 -> 364.9 mm, vias 247 -> 246
- net TX_MOSI: track 37.7 -> 40.6 mm
- net N$40: track 202.9 -> 205.7 mm
- net TX_RST: track 55.3 -> 57.9 mm
- net TX_MISO: track 41.5 -> 44.0 mm
- net SWDIO: track 88.8 -> 86.3 mm
- net TX_CLK: track 39.7 -> 41.9 mm
- net RX_CS: track 70.8 -> 69.6 mm
- net N$24: track 42.2 -> 41.0 mm
- net TC/RX/CS: track 33.9 -> 32.7 mm
- net TX_GPIO0: track 48.5 -> 49.6 mm
- net TX_CS: track 66.4 -> 67.4 mm
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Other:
- board text added: "!RST"
- board text added: "RXD"
- board text added: "TXD"
